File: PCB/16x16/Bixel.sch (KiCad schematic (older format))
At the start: 256 parts

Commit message: Starting the wiring in the schematic
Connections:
- net COL_0: now also B1.10 (COL), B10.10 (COL), B11.10 (COL), B12.10 (COL), B13.10 (COL), B14.10 (COL), B15.10 (COL), B16.10 (COL), B2.10 (COL), B3.10 (COL), B4.10 (COL), B5.10 (COL)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
- net COL_1: now also B17.10 (COL), B18.10 (COL), B19.10 (COL), B20.10 (COL), B21.10 (COL), B22.10 (COL), B23.10 (COL), B24.10 (COL), B25.10 (COL), B26.10 (COL), B27.10 (COL), B28.10 (COL)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
- net COL_10: now also B161.10 (COL), B162.10 (COL), B163.10 (COL), B164.10 (COL), B165.10 (COL), B166.10 (COL), B167.10 (COL), B168.10 (COL), B169.10 (COL), B170.10 (COL), B171.10 (COL), B172.10 (COL)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
- net COL_11: now also B177.10 (COL), B178.10 (COL), B179.10 (COL), B180.10 (COL), B181.10 (COL), B182.10 (COL), B183.10 (COL), B184.10 (COL), B185.10 (COL), B186.10 (COL), B187.10 (COL), B188.10 (COL)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
- net COL_12: now also B193.10 (COL), B194.10 (COL), B195.10 (COL), B196.10 (COL), B197.10 (COL), B198.10 (COL), B199.10 (COL), B200.10 (COL), B201.10 (COL), B202.10 (COL), B203.10 (COL), B204.10 (COL)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
- net COL_13: now also B209.10 (COL), B210.10 (COL), B211.10 (COL), B212.10 (COL), B213.10 (COL), B214.10 (COL), B215.10 (COL), B216.10 (COL), B217.10 (COL), B218.10 (COL), B219.10 (COL), B220.10 (COL)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
- net COL_14: now also B225.10 (COL), B226.10 (COL), B227.10 (COL), B228.10 (COL), B229.10 (COL), B230.10 (COL), B231.10 (COL), B232.10 (COL), B233.10 (COL), B234.10 (COL), B235.10 (COL), B236.10 (COL)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
- net COL_15: now also B241.10 (COL), B242.10 (COL), B243.10 (COL), B244.10 (COL), B245.10 (COL), B246.10 (COL), B247.10 (COL), B248.10 (COL), B249.10 (COL), B250.10 (COL), B251.10 (COL), B252.10 (COL)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
- net COL_2: now also B33.10 (COL), B34.10 (COL), B35.10 (COL), B36.10 (COL), B37.10 (COL), B38.10 (COL), B39.10 (COL), B40.10 (COL), B41.10 (COL), B42.10 (COL), B43.10 (COL), B44.10 (COL)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
- net COL_3: now also B49.10 (COL), B50.10 (COL), B51.10 (COL), B52.10 (COL), B53.10 (COL), B54.10 (COL), B55.10 (COL), B56.10 (COL), B57.10 (COL), B58.10 (COL), B59.10 (COL), B60.10 (COL)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
- net COL_4: now also B65.10 (COL), B66.10 (COL), B67.10 (COL), B68.10 (COL), B69.10 (COL), B70.10 (COL), B71.10 (COL), B72.10 (COL), B73.10 (COL), B74.10 (COL), B75.10 (COL), B76.10 (COL)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
- net COL_5: now also B81.10 (COL), B82.10 (COL), B83.10 (COL), B84.10 (COL), B85.10 (COL), B86.10 (COL), B87.10 (COL), B88.10 (COL), B89.10 (COL), B90.10 (COL), B91.10 (COL), B92.10 (COL)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
- net COL_6: now also B100.10 (COL), B101.10 (COL), B102.10 (COL), B103.10 (COL), B104.10 (COL), B105.10 (COL), B106.10 (COL), B107.10 (COL), B108.10 (COL), B109.10 (COL), B110.10 (COL), B111.10 (COL)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
- net COL_7: now also B113.10 (COL), B114.10 (COL), B115.10 (COL), B116.10 (COL), B117.10 (COL), B118.10 (COL), B119.10 (COL), B120.10 (COL), B121.10 (COL), B122.10 (COL), B123.10 (COL), B124.10 (COL)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
- net COL_8: now also B129.10 (COL), B130.10 (COL), B131.10 (COL), B132.10 (COL), B133.10 (COL), B134.10 (COL), B135.10 (COL), B136.10 (COL), B137.10 (COL), B138.10 (COL), B139.10 (COL), B140.10 (COL)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
- net COL_9: now also B145.10 (COL), B146.10 (COL), B147.10 (COL), B148.10 (COL), B149.10 (COL), B150.10 (COL), B151.10 (COL), B152.10 (COL), B153.10 (COL), B154.10 (COL), B155.10 (COL), B156.10 (COL)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
- net ROW_0: now also B1.9 (ROW), B113.9 (ROW), B129.9 (ROW), B145.9 (ROW), B161.9 (ROW), B17.9 (ROW), B177.9 (ROW), B193.9 (ROW), B209.9 (ROW), B225.9 (ROW), B241.9 (ROW), B33.9 (ROW)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
- net ROW_1: now also B114.9 (ROW), B130.9 (ROW), B146.9 (ROW), B162.9 (ROW), B178.9 (ROW), B18.9 (ROW), B194.9 (ROW), B2.9 (ROW), B210.9 (ROW), B226.9 (ROW), B242.9 (ROW), B34.9 (ROW)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
- net ROW_10: now also B107.9 (ROW), B11.9 (ROW), B123.9 (ROW), B139.9 (ROW), B155.9 (ROW), B171.9 (ROW), B187.9 (ROW), B203.9 (ROW), B219.9 (ROW), B235.9 (ROW), B251.9 (ROW), B27.9 (ROW)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
- net ROW_11: now also B108.9 (ROW), B12.9 (ROW), B124.9 (ROW), B140.9 (ROW), B156.9 (ROW), B172.9 (ROW), B188.9 (ROW), B204.9 (ROW), B220.9 (ROW), B236.9 (ROW), B252.9 (ROW), B28.9 (ROW)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
- net ROW_12: now also B109.9 (ROW), B125.9 (ROW), B13.9 (ROW), B157.9 (ROW), B173.9 (ROW), B189.9 (ROW), B205.9 (ROW), B221.9 (ROW), B237.9 (ROW), B253.9 (ROW), B29.9 (ROW), B45.9 (ROW)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
- net ROW_13: now also B110.9 (ROW), B126.9 (ROW), B14.9 (ROW), B142.9 (ROW), B158.9 (ROW), B174.9 (ROW), B190.9 (ROW), B206.9 (ROW), B222.9 (ROW), B238.9 (ROW), B254.9 (ROW), B30.9 (ROW)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
- net ROW_14: now also B111.9 (ROW), B127.9 (ROW), B143.9 (ROW), B15.9 (ROW), B159.9 (ROW), B175.9 (ROW), B191.9 (ROW), B207.9 (ROW), B223.9 (ROW), B239.9 (ROW), B255.9 (ROW), B31.9 (ROW)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
- net ROW_15: now also B112.9 (ROW), B128.9 (ROW), B144.9 (ROW), B16.9 (ROW), B160.9 (ROW), B176.9 (ROW), B192.9 (ROW), B208.9 (ROW), B224.9 (ROW), B240.9 (ROW), B256.9 (ROW), B32.9 (ROW)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
- net ROW_2: now also B115.9 (ROW), B131.9 (ROW), B147.9 (ROW), B163.9 (ROW), B179.9 (ROW), B19.9 (ROW), B195.9 (ROW), B211.9 (ROW), B227.9 (ROW), B243.9 (ROW), B3.9 (ROW), B35.9 (ROW)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
- net ROW_3: now also B100.9 (ROW), B116.9 (ROW), B132.9 (ROW), B148.9 (ROW), B164.9 (ROW), B180.9 (ROW), B196.9 (ROW), B20.9 (ROW), B212.9 (ROW), B228.9 (ROW), B244.9 (ROW), B36.9 (ROW)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
- net ROW_4: now also B101.9 (ROW), B117.9 (ROW), B133.9 (ROW), B149.9 (ROW), B165.9 (ROW), B181.9 (ROW), B197.9 (ROW), B21.9 (ROW), B213.9 (ROW), B229.9 (ROW), B245.9 (ROW), B37.9 (ROW)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
- net ROW_5: now also B102.9 (ROW), B118.9 (ROW), B134.9 (ROW), B150.9 (ROW), B166.9 (ROW), B182.9 (ROW), B198.9 (ROW), B214.9 (ROW), B22.9 (ROW), B230.9 (ROW), B246.9 (ROW), B38.9 (ROW)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
- net ROW_6: now also B103.9 (ROW), B119.9 (ROW), B135.9 (ROW), B151.9 (ROW), B167.9 (ROW), B183.9 (ROW), B199.9 (ROW), B215.9 (ROW), B23.9 (ROW), B231.9 (ROW), B247.9 (ROW), B39.9 (ROW)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
- net ROW_7: now also B104.9 (ROW), B120.9 (ROW), B136.9 (ROW), B152.9 (ROW), B168.9 (ROW), B184.9 (ROW), B200.9 (ROW), B216.9 (ROW), B232.9 (ROW), B24.9 (ROW), B248.9 (ROW), B40.9 (ROW)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
- net ROW_8: now also B105.9 (ROW), B121.9 (ROW), B137.9 (ROW), B153.9 (ROW), B169.9 (ROW), B185.9 (ROW), B201.9 (ROW), B217.9 (ROW), B233.9 (ROW), B249.9 (ROW), B25.9 (ROW), B41.9 (ROW)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
- net ROW_9: now also B10.9 (ROW), B106.9 (ROW), B122.9 (ROW), B138.9 (ROW), B154.9 (ROW), B170.9 (ROW), B186.9 (ROW), B202.9 (ROW), B218.9 (ROW), B234.9 (ROW), B250.9 (ROW), B26.9 (ROW)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
- net at B1.5 (VCC): now also B2.1 (VCC)
- net at B1.6 (CO): now also B2.2 (CI)
- net at B1.7 (DO): now also B2.3 (DI)
- net at B1.8 (GND): now also B2.4 (GND)
- net at B2.5 (VCC): now also B3.1 (VCC)
- net at B2.6 (CO): now also B3.2 (CI)
- net at B2.7 (DO): now also B3.3 (DI)
- net at B2.8 (GND): now also B3.4 (GND)
- net at B3.5 (VCC): now also B4.1 (VCC)
- net at B3.6 (CO): now also B4.2 (CI)
- net at B3.7 (DO): now also B4.3 (DI)
- net at B3.8 (GND): now also B4.4 (GND)
- net at B4.5 (VCC): now also B5.1 (VCC)
- net at B4.6 (CO): now also B5.2 (CI)
- net at B4.7 (DO): now also B5.3 (DI)
- net at B4.8 (GND): now also B5.4 (GND)
- net at B5.5 (VCC): now also B6.1 (VCC)
- net at B5.6 (CO): now also B6.2 (CI)
- net at B5.7 (DO): now also B6.3 (DI)
- net at B5.8 (GND): now also B6.4 (GND)
- net at B6.5 (VCC): now also B7.1 (VCC)
- net at B6.6 (CO): now also B7.2 (CI)
- net at B6.7 (DO): now also B7.3 (DI)
- net at B6.8 (GND): now also B7.4 (GND)
- net at B7.5 (VCC): now also B8.1 (VCC)
- net at B7.6 (CO): now also B8.2 (CI)
- net at B7.7 (DO): now also B8.3 (DI)
- net at B7.8 (GND): now also B8.4 (GND)
- net at B8.5 (VCC): now also B9.1 (VCC)
- net at B8.6 (CO): now also B9.2 (CI)
- net at B8.7 (DO): now also B9.3 (DI)
- net at B8.8 (GND): now also B9.4 (GND)
- net at B9.5 (VCC): now also B10.1 (VCC)
- net at B9.6 (CO): now also B10.2 (CI)
- net at B9.7 (DO): now also B10.3 (DI)
- net at B9.8 (GND): now also B10.4 (GND)
- net at B10.5 (VCC): now also B11.1 (VCC)
- net at B10.6 (CO): now also B11.2 (CI)
- net at B10.7 (DO): now also B11.3 (DI)
- net at B10.8 (GND): now also B11.4 (GND)
- net at B11.5 (VCC): now also B12.1 (VCC)
- net at B11.6 (CO): now also B12.2 (CI)
- net at B11.7 (DO): now also B12.3 (DI)
- net at B11.8 (GND): now also B12.4 (GND)
- net at B12.5 (VCC): now also B13.1 (VCC)
- net at B12.6 (CO): now also B13.2 (CI)
- net at B12.7 (DO): now also B13.3 (DI)
- net at B12.8 (GND): now also B13.4 (GND)
- net at B13.5 (VCC): now also B14.1 (VCC)
- net at B13.6 (CO): now also B14.2 (CI)
- net at B13.7 (DO): now also B14.3 (DI)
- net at B13.8 (GND): now also B14.4 (GND)
- net at B14.5 (VCC): now also B15.1 (VCC)
- net at B14.6 (CO): now also B15.2 (CI)
- net at B14.7 (DO): now also B15.3 (DI)
- net at B14.8 (GND): now also B15.4 (GND)
- net at B15.5 (VCC): now also B16.1 (VCC)
- net at B15.6 (CO): now also B16.2 (CI)
- net at B15.7 (DO): now also B16.3 (DI)
- net at B15.8 (GND): now also B16.4 (GND)
- net at B16.5 (VCC): now also B32.8 (VCC)
- net at B16.6 (CO): now also B32.7 (CI)
- net at B16.7 (DO): now also B32.6 (DI)
- net at B16.8 (GND): now also B32.5 (GND)
- net at B17.1 (GND): now also B33.4 (GND)
- net at B17.2 (DO): now also B33.3 (DI)
- net at B17.3 (CO): now also B33.2 (CI)
- net at B17.4 (VCC): now also B33.1 (VCC)
- net at B17.5 (GND): now also B18.1 (GND)
- net at B17.6 (DI): now also B18.2 (DO)
- net at B17.7 (CI): now also B18.3 (CO)
- net at B17.8 (VCC): now also B18.4 (VCC)
- net at B18.5 (GND): now also B19.1 (GND)
- net at B18.6 (DI): now also B19.2 (DO)
- net at B18.7 (CI): now also B19.3 (CO)
- net at B18.8 (VCC): now also B19.4 (VCC)
- net at B19.5 (GND): now also B20.1 (GND)
- net at B19.6 (DI): now also B20.2 (DO)
- net at B19.7 (CI): now also B20.3 (CO)
- net at B19.8 (VCC): now also B20.4 (VCC)
- net at B20.5 (GND): now also B21.1 (GND)
- net at B20.6 (DI): now also B21.2 (DO)
- net at B20.7 (CI): now also B21.3 (CO)
- net at B20.8 (VCC): now also B21.4 (VCC)
- net at B21.5 (GND): now also B22.1 (GND)
- net at B21.6 (DI): now also B22.2 (DO)
- net at B21.7 (CI): now also B22.3 (CO)
- net at B21.8 (VCC): now also B22.4 (VCC)
- net at B22.5 (GND): now also B23.1 (GND)
- net at B22.6 (DI): now also B23.2 (DO)
- net at B22.7 (CI): now also B23.3 (CO)
- net at B22.8 (VCC): now also B23.4 (VCC)
- net at B23.5 (GND): now also B24.1 (GND)
- net at B23.6 (DI): now also B24.2 (DO)
- net at B23.7 (CI): now also B24.3 (CO)
- net at B23.8 (VCC): now also B24.4 (VCC)
- net at B24.5 (GND): now also B25.1 (GND)
- net at B24.6 (DI): now also B25.2 (DO)
- net at B24.7 (CI): now also B25.3 (CO)
- net at B24.8 (VCC): now also B25.4 (VCC)
- net at B25.5 (GND): now also B26.1 (GND)
- net at B25.6 (DI): now also B26.2 (DO)
- net at B25.7 (CI): now also B26.3 (CO)
- net at B25.8 (VCC): now also B26.4 (VCC)
- net at B26.5 (GND): now also B27.1 (GND)
- net at B26.6 (DI): now also B27.2 (DO)
- net at B26.7 (CI): now also B27.3 (CO)
- net at B26.8 (VCC): now also B27.4 (VCC)
- net at B27.5 (GND): now also B28.1 (GND)
- net at B27.6 (DI): now also B28.2 (DO)
- net at B27.7 (CI): now also B28.3 (CO)
- net at B27.8 (VCC): now also B28.4 (VCC)
- net at B28.5 (GND): now also B29.1 (GND)
- net at B28.6 (DI): now also B29.2 (DO)
- net at B28.7 (CI): now also B29.3 (CO)
- net at B28.8 (VCC): now also B29.4 (VCC)
- net at B29.5 (GND): now also B30.1 (GND)
- net at B29.6 (DI): now also B30.2 (DO)
- net at B29.7 (CI): now also B30.3 (CO)
- net at B29.8 (VCC): now also B30.4 (VCC)
- net at B30.5 (GND): now also B31.1 (GND)
- net at B30.6 (DI): now also B31.2 (DO)
- net at B30.7 (CI): now also B31.3 (CO)
- net at B30.8 (VCC): now also B31.4 (VCC)
- net at B31.5 (GND): now also B32.1 (GND)
- net at B31.6 (DI): now also B32.2 (DO)
- net at B31.7 (CI): now also B32.3 (CO)
- net at B31.8 (VCC): now also B32.4 (VCC)
- net at B33.5 (VCC): now also B34.1 (VCC)
- net at B33.6 (CO): now also B34.2 (CI)
- net at B33.7 (DO): now also B34.3 (DI)
- net at B33.8 (GND): now also B34.4 (GND)
- net at B34.5 (VCC): now also B35.1 (VCC)
- net at B34.6 (CO): now also B35.2 (CI)
- net at B34.7 (DO): now also B35.3 (DI)
- net at B34.8 (GND): now also B35.4 (GND)
- net at B35.5 (VCC): now also B36.1 (VCC)
- net at B35.6 (CO): now also B36.2 (CI)
- net at B35.7 (DO): now also B36.3 (DI)
- net at B35.8 (GND): now also B36.4 (GND)
- net at B36.5 (VCC): now also B37.1 (VCC)
- net at B36.6 (CO): now also B37.2 (CI)
- net at B36.7 (DO): now also B37.3 (DI)
- net at B36.8 (GND): now also B37.4 (GND)
- net at B37.5 (VCC): now also B38.1 (VCC)
- net at B37.6 (CO): now also B38.2 (CI)
- net at B37.7 (DO): now also B38.3 (DI)
- net at B37.8 (GND): now also B38.4 (GND)
- net at B38.5 (VCC): now also B39.1 (VCC)
- net at B38.6 (CO): now also B39.2 (CI)
- net at B38.7 (DO): now also B39.3 (DI)
- net at B38.8 (GND): now also B39.4 (GND)
- net at B39.5 (VCC): now also B40.1 (VCC)
- net at B39.6 (CO): now also B40.2 (CI)
- net at B39.7 (DO): now also B40.3 (DI)
- net at B39.8 (GND): now also B40.4 (GND)
- net at B40.5 (VCC): now also B41.1 (VCC)
- net at B40.6 (CO): now also B41.2 (CI)
- net at B40.7 (DO): now also B41.3 (DI)
- net at B40.8 (GND): now also B41.4 (GND)
- net at B41.5 (VCC): now also B42.1 (VCC)
- net at B41.6 (CO): now also B42.2 (CI)
- net at B41.7 (DO): now also B42.3 (DI)
- net at B41.8 (GND): now also B42.4 (GND)
- net at B42.5 (VCC): now also B43.1 (VCC)
- net at B42.6 (CO): now also B43.2 (CI)
- net at B42.7 (DO): now also B43.3 (DI)
- net at B42.8 (GND): now also B43.4 (GND)
- net at B43.5 (VCC): now also B44.1 (VCC)
- net at B43.6 (CO): now also B44.2 (CI)
- net at B43.7 (DO): now also B44.3 (DI)
- net at B43.8 (GND): now also B44.4 (GND)
- net at B44.5 (VCC): now also B45.1 (VCC)
- net at B44.6 (CO): now also B45.2 (CI)
- net at B44.7 (DO): now also B45.3 (DI)
- net at B44.8 (GND): now also B45.4 (GND)
- net at B45.5 (VCC): now also B46.1 (VCC)
- net at B45.6 (CO): now also B46.2 (CI)
- net at B45.7 (DO): now also B46.3 (DI)
- net at B45.8 (GND): now also B46.4 (GND)
- net at B46.5 (VCC): now also B47.1 (VCC)
- net at B46.6 (CO): now also B47.2 (CI)
- net at B46.7 (DO): now also B47.3 (DI)
- net at B46.8 (GND): now also B47.4 (GND)
- net at B47.5 (VCC): now also B48.1 (VCC)
- net at B47.6 (CO): now also B48.2 (CI)
- net at B47.7 (DO): now also B48.3 (DI)
- net at B47.8 (GND): now also B48.4 (GND)
- net at B48.5 (VCC): now also B64.8 (VCC)
- net at B48.6 (CO): now also B64.7 (CI)
- net at B48.7 (DO): now also B64.6 (DI)
- net at B48.8 (GND): now also B64.5 (GND)
- net at B49.1 (GND): now also B65.4 (GND)
- net at B49.2 (DO): now also B65.3 (DI)
- net at B49.3 (CO): now also B65.2 (CI)
- net at B49.4 (VCC): now also B65.1 (VCC)
- net at B49.5 (GND): now also B50.1 (GND)
- net at B49.6 (DI): now also B50.2 (DO)
- net at B49.7 (CI): now also B50.3 (CO)
- net at B49.8 (VCC): now also B50.4 (VCC)
- net at B50.5 (GND): now also B51.1 (GND)
- net at B50.6 (DI): now also B51.2 (DO)
- net at B50.7 (CI): now also B51.3 (CO)
- net at B50.8 (VCC): now also B51.4 (VCC)
- net at B51.5 (GND): now also B52.1 (GND)
- net at B51.6 (DI): now also B52.2 (DO)
- net at B51.7 (CI): now also B52.3 (CO)
- net at B51.8 (VCC): now also B52.4 (VCC)
- net at B52.5 (GND): now also B53.1 (GND)
- net at B52.6 (DI): now also B53.2 (DO)
- net at B52.7 (CI): now also B53.3 (CO)
- net at B52.8 (VCC): now also B53.4 (VCC)
- net at B53.5 (GND): now also B54.1 (GND)
- net at B53.6 (DI): now also B54.2 (DO)
- net at B53.7 (CI): now also B54.3 (CO)
- net at B53.8 (VCC): now also B54.4 (VCC)
- net at B54.5 (GND): now also B55.1 (GND)
- net at B54.6 (DI): now also B55.2 (DO)
- net at B54.7 (CI): now also B55.3 (CO)
- net at B54.8 (VCC): now also B55.4 (VCC)
- net at B55.5 (GND): now also B56.1 (GND)
- net at B55.6 (DI): now also B56.2 (DO)
- net at B55.7 (CI): now also B56.3 (CO)
- net at B55.8 (VCC): now also B56.4 (VCC)
- net at B56.5 (GND): now also B57.1 (GND)
- net at B56.6 (DI): now also B57.2 (DO)
- net at B56.7 (CI): now also B57.3 (CO)
- net at B56.8 (VCC): now also B57.4 (VCC)
- net at B57.5 (GND): now also B58.1 (GND)
- net at B57.6 (DI): now also B58.2 (DO)
- net at B57.7 (CI): now also B58.3 (CO)
- net at B57.8 (VCC): now also B58.4 (VCC)
- net at B58.5 (GND): now also B59.1 (GND)
- net at B58.6 (DI): now also B59.2 (DO)
- net at B58.7 (CI): now also B59.3 (CO)
- net at B58.8 (VCC): now also B59.4 (VCC)
- net at B59.5 (GND): now also B60.1 (GND)
- net at B59.6 (DI): now also B60.2 (DO)
- net at B59.7 (CI): now also B60.3 (CO)
- net at B59.8 (VCC): now also B60.4 (VCC)
- net at B60.5 (GND): now also B61.1 (GND)
- net at B60.6 (DI): now also B61.2 (DO)
- net at B60.7 (CI): now also B61.3 (CO)
- net at B60.8 (VCC): now also B61.4 (VCC)
- net at B61.5 (GND): now also B62.1 (GND)
- net at B61.6 (DI): now also B62.2 (DO)
- net at B61.7 (CI): now also B62.3 (CO)
- net at B61.8 (VCC): now also B62.4 (VCC)
- net at B62.5 (GND): now also B63.1 (GND)
- net at B62.6 (DI): now also B63.2 (DO)
- net at B62.7 (CI): now also B63.3 (CO)
- net at B62.8 (VCC): now also B63.4 (VCC)
- net at B63.5 (GND): now also B64.1 (GND)
- net at B63.6 (DI): now also B64.2 (DO)
- net at B63.7 (CI): now also B64.3 (CO)
- net at B63.8 (VCC): now also B64.4 (VCC)
- net at B65.5 (VCC): now also B66.1 (VCC)
- net at B65.6 (CO): now also B66.2 (CI)
- net at B65.7 (DO): now also B66.3 (DI)
- net at B65.8 (GND): now also B66.4 (GND)
- net at B66.5 (VCC): now also B67.1 (VCC)
- net at B66.6 (CO): now also B67.2 (CI)
- net at B66.7 (DO): now also B67.3 (DI)
- net at B66.8 (GND): now also B67.4 (GND)
- net at B67.5 (VCC): now also B68.1 (VCC)
- net at B67.6 (CO): now also B68.2 (CI)
- net at B67.7 (DO): now also B68.3 (DI)
- net at B67.8 (GND): now also B68.4 (GND)
- net at B68.5 (VCC): now also B69.1 (VCC)
- net at B68.6 (CO): now also B69.2 (CI)
- net at B68.7 (DO): now also B69.3 (DI)
- net at B68.8 (GND): now also B69.4 (GND)
- net at B69.5 (VCC): now also B70.1 (VCC)
- net at B69.6 (CO): now also B70.2 (CI)
- net at B69.7 (DO): now also B70.3 (DI)
- net at B69.8 (GND): now also B70.4 (GND)
- net at B70.5 (VCC): now also B71.1 (VCC)
- net at B70.6 (CO): now also B71.2 (CI)
- net at B70.7 (DO): now also B71.3 (DI)
- net at B70.8 (GND): now also B71.4 (GND)
- net at B71.5 (VCC): now also B72.1 (VCC)
- net at B71.6 (CO): now also B72.2 (CI)
- net at B71.7 (DO): now also B72.3 (DI)
- net at B71.8 (GND): now also B72.4 (GND)
- net at B72.5 (VCC): now also B73.1 (VCC)
- net at B72.6 (CO): now also B73.2 (CI)
- net at B72.7 (DO): now also B73.3 (DI)
- net at B72.8 (GND): now also B73.4 (GND)
- net at B73.5 (VCC): now also B74.1 (VCC)
- net at B73.6 (CO): now also B74.2 (CI)
- net at B73.7 (DO): now also B74.3 (DI)
- net at B73.8 (GND): now also B74.4 (GND)
- net at B74.5 (VCC): now also B75.1 (VCC)
- net at B74.6 (CO): now also B75.2 (CI)
- net at B74.7 (DO): now also B75.3 (DI)
- net at B74.8 (GND): now also B75.4 (GND)
- net at B75.5 (VCC): now also B76.1 (VCC)
- net at B75.6 (CO): now also B76.2 (CI)
- net at B75.7 (DO): now also B76.3 (DI)
- net at B75.8 (GND): now also B76.4 (GND)
- net at B76.5 (VCC): now also B77.1 (VCC)
- net at B76.6 (CO): now also B77.2 (CI)
- net at B76.7 (DO): now also B77.3 (DI)
- net at B76.8 (GND): now also B77.4 (GND)
- net at B77.5 (VCC): now also B78.1 (VCC)
- net at B77.6 (CO): now also B78.2 (CI)
- net at B77.7 (DO): now also B78.3 (DI)
- net at B77.8 (GND): now also B78.4 (GND)
- net at B78.5 (VCC): now also B79.1 (VCC)
- net at B78.6 (CO): now also B79.2 (CI)
- net at B78.7 (DO): now also B79.3 (DI)
- net at B78.8 (GND): now also B79.4 (GND)
- net at B79.5 (VCC): now also B80.1 (VCC)
- net at B79.6 (CO): now also B80.2 (CI)
- net at B79.7 (DO): now also B80.3 (DI)
- net at B79.8 (GND): now also B80.4 (GND)
- net at B80.5 (VCC): now also B96.8 (VCC)
- net at B80.6 (CO): now also B96.7 (CI)
- net at B80.7 (DO): now also B96.6 (DI)
- net at B80.8 (GND): now also B96.5 (GND)
- net at B81.1 (GND): now also B97.4 (GND)
- net at B81.2 (DO): now also B97.3 (DI)
- net at B81.3 (CO): now also B97.2 (CI)
- net at B81.4 (VCC): now also B97.1 (VCC)
- net at B81.5 (GND): now also B82.1 (GND)
- net at B81.6 (DI): now also B82.2 (DO)
- net at B81.7 (CI): now also B82.3 (CO)
- net at B81.8 (VCC): now also B82.4 (VCC)
- net at B82.5 (GND): now also B83.1 (GND)
- net at B82.6 (DI): now also B83.2 (DO)
- net at B82.7 (CI): now also B83.3 (CO)
- net at B82.8 (VCC): now also B83.4 (VCC)
- net at B83.5 (GND): now also B84.1 (GND)
- net at B83.6 (DI): now also B84.2 (DO)
- net at B83.7 (CI): now also B84.3 (CO)
- net at B83.8 (VCC): now also B84.4 (VCC)
- net at B84.5 (GND): now also B85.1 (GND)
- net at B84.6 (DI): now also B85.2 (DO)
- net at B84.7 (CI): now also B85.3 (CO)
- net at B84.8 (VCC): now also B85.4 (VCC)
- net at B85.5 (GND): now also B86.1 (GND)
- net at B85.6 (DI): now also B86.2 (DO)
- net at B85.7 (CI): now also B86.3 (CO)
- net at B85.8 (VCC): now also B86.4 (VCC)
- net at B86.5 (GND): now also B87.1 (GND)
- net at B86.6 (DI): now also B87.2 (DO)
- net at B86.7 (CI): now also B87.3 (CO)
- net at B86.8 (VCC): now also B87.4 (VCC)
- net at B87.5 (GND): now also B88.1 (GND)
- net at B87.6 (DI): now also B88.2 (DO)
- net at B87.7 (CI): now also B88.3 (CO)
- net at B87.8 (VCC): now also B88.4 (VCC)
- net at B88.5 (GND): now also B89.1 (GND)
- net at B88.6 (DI): now also B89.2 (DO)
- net at B88.7 (CI): now also B89.3 (CO)
- net at B88.8 (VCC): now also B89.4 (VCC)
- net at B89.5 (GND): now also B90.1 (GND)
- net at B89.6 (DI): now also B90.2 (DO)
- net at B89.7 (CI): now also B90.3 (CO)
- net at B89.8 (VCC): now also B90.4 (VCC)
- net at B90.5 (GND): now also B91.1 (GND)
- net at B90.6 (DI): now also B91.2 (DO)
- net at B90.7 (CI): now also B91.3 (CO)
- net at B90.8 (VCC): now also B91.4 (VCC)
- net at B91.5 (GND): now also B92.1 (GND)
- net at B91.6 (DI): now also B92.2 (DO)
- net at B91.7 (CI): now also B92.3 (CO)
- net at B91.8 (VCC): now also B92.4 (VCC)
- net at B92.5 (GND): now also B93.1 (GND)
- net at B92.6 (DI): now also B93.2 (DO)
- net at B92.7 (CI): now also B93.3 (CO)
- net at B92.8 (VCC): now also B93.4 (VCC)
- net at B93.5 (GND): now also B94.1 (GND)
- net at B93.6 (DI): now also B94.2 (DO)
- net at B93.7 (CI): now also B94.3 (CO)
- net at B93.8 (VCC): now also B94.4 (VCC)
- net at B94.5 (GND): now also B95.1 (GND)
- net at B94.6 (DI): now also B95.2 (DO)
- net at B94.7 (CI): now also B95.3 (CO)
- net at B94.8 (VCC): now also B95.4 (VCC)
- net at B95.5 (GND): now also B96.1 (GND)
- net at B95.6 (DI): now also B96.2 (DO)
- net at B95.7 (CI): now also B96.3 (CO)
- net at B95.8 (VCC): now also B96.4 (VCC)
- net at B97.5 (VCC): now also B98.1 (VCC)
- net at B97.6 (CO): now also B98.2 (CI)
- net at B97.7 (DO): now also B98.3 (DI)
- net at B97.8 (GND): now also B98.4 (GND)
- net at B98.5 (VCC): now also B99.1 (VCC)
- net at B98.6 (CO): now also B99.2 (CI)
- net at B98.7 (DO): now also B99.3 (DI)
- net at B98.8 (GND): now also B99.4 (GND)
- net at B99.5 (VCC): now also B100.1 (VCC)
- net at B99.6 (CO): now also B100.2 (CI)
- net at B99.7 (DO): now also B100.3 (DI)
- net at B99.8 (GND): now also B100.4 (GND)
- net at B100.5 (VCC): now also B101.1 (VCC)
- net at B100.6 (CO): now also B101.2 (CI)
- net at B100.7 (DO): now also B101.3 (DI)
- net at B100.8 (GND): now also B101.4 (GND)
- net at B101.5 (VCC): now also B102.1 (VCC)
- net at B101.6 (CO): now also B102.2 (CI)
- net at B101.7 (DO): now also B102.3 (DI)
- net at B101.8 (GND): now also B102.4 (GND)
- net at B102.5 (VCC): now also B103.1 (VCC)
- net at B102.6 (CO): now also B103.2 (CI)
- net at B102.7 (DO): now also B103.3 (DI)
- net at B102.8 (GND): now also B103.4 (GND)
- net at B103.5 (VCC): now also B104.1 (VCC)
- net at B103.6 (CO): now also B104.2 (CI)
- net at B103.7 (DO): now also B104.3 (DI)
- net at B103.8 (GND): now also B104.4 (GND)
- net at B104.5 (VCC): now also B105.1 (VCC)
- net at B104.6 (CO): now also B105.2 (CI)
- net at B104.7 (DO): now also B105.3 (DI)
- net at B104.8 (GND): now also B105.4 (GND)
- net at B105.5 (VCC): now also B106.1 (VCC)
- net at B105.6 (CO): now also B106.2 (CI)
- net at B105.7 (DO): now also B106.3 (DI)
- net at B105.8 (GND): now also B106.4 (GND)
- net at B106.5 (VCC): now also B107.1 (VCC)
- net at B106.6 (CO): now also B107.2 (CI)
- net at B106.7 (DO): now also B107.3 (DI)
- net at B106.8 (GND): now also B107.4 (GND)
- net at B107.5 (VCC): now also B108.1 (VCC)
- net at B107.6 (CO): now also B108.2 (CI)
- net at B107.7 (DO): now also B108.3 (DI)
- net at B107.8 (GND): now also B108.4 (GND)
- net at B108.5 (VCC): now also B109.1 (VCC)
- net at B108.6 (CO): now also B109.2 (CI)
- net at B108.7 (DO): now also B109.3 (DI)
- net at B108.8 (GND): now also B109.4 (GND)
- net at B109.5 (VCC): now also B110.1 (VCC)
- net at B109.6 (CO): now also B110.2 (CI)
- net at B109.7 (DO): now also B110.3 (DI)
- net at B109.8 (GND): now also B110.4 (GND)
- net at B110.5 (VCC): now also B111.1 (VCC)
- net at B110.6 (CO): now also B111.2 (CI)
- net at B110.7 (DO): now also B111.3 (DI)
- net at B110.8 (GND): now also B111.4 (GND)
- net at B111.5 (VCC): now also B112.1 (VCC)
- net at B111.6 (CO): now also B112.2 (CI)
- net at B111.7 (DO): now also B112.3 (DI)
- net at B111.8 (GND): now also B112.4 (GND)
- net at B112.5 (VCC): now also B128.8 (VCC)
- net at B112.6 (CO): now also B128.7 (CI)
- net at B112.7 (DO): now also B128.6 (DI)
- net at B112.8 (GND): now also B128.5 (GND)
- net at B113.1 (GND): now also B129.4 (GND)
- net at B113.2 (DO): now also B129.3 (DI)
- net at B113.3 (CO): now also B129.2 (CI)
- net at B113.4 (VCC): now also B129.1 (VCC)
- net at B113.5 (GND): now also B114.1 (GND)
- net at B113.6 (DI): now also B114.2 (DO)
- net at B113.7 (CI): now also B114.3 (CO)
- net at B113.8 (VCC): now also B114.4 (VCC)
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
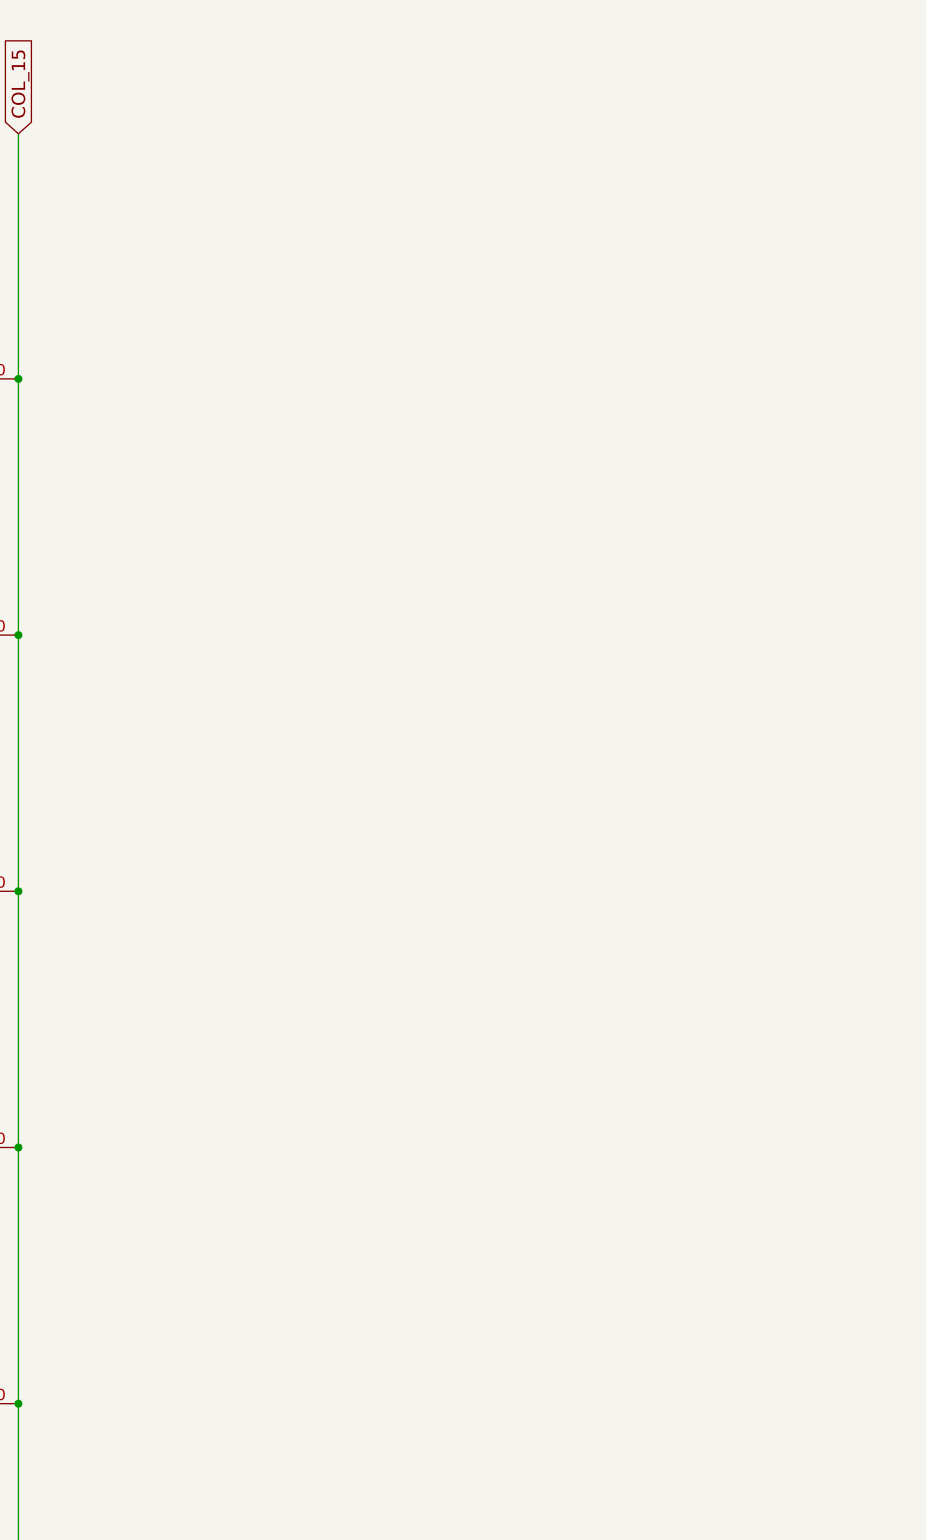
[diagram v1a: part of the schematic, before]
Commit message: Shift Register schematic layout
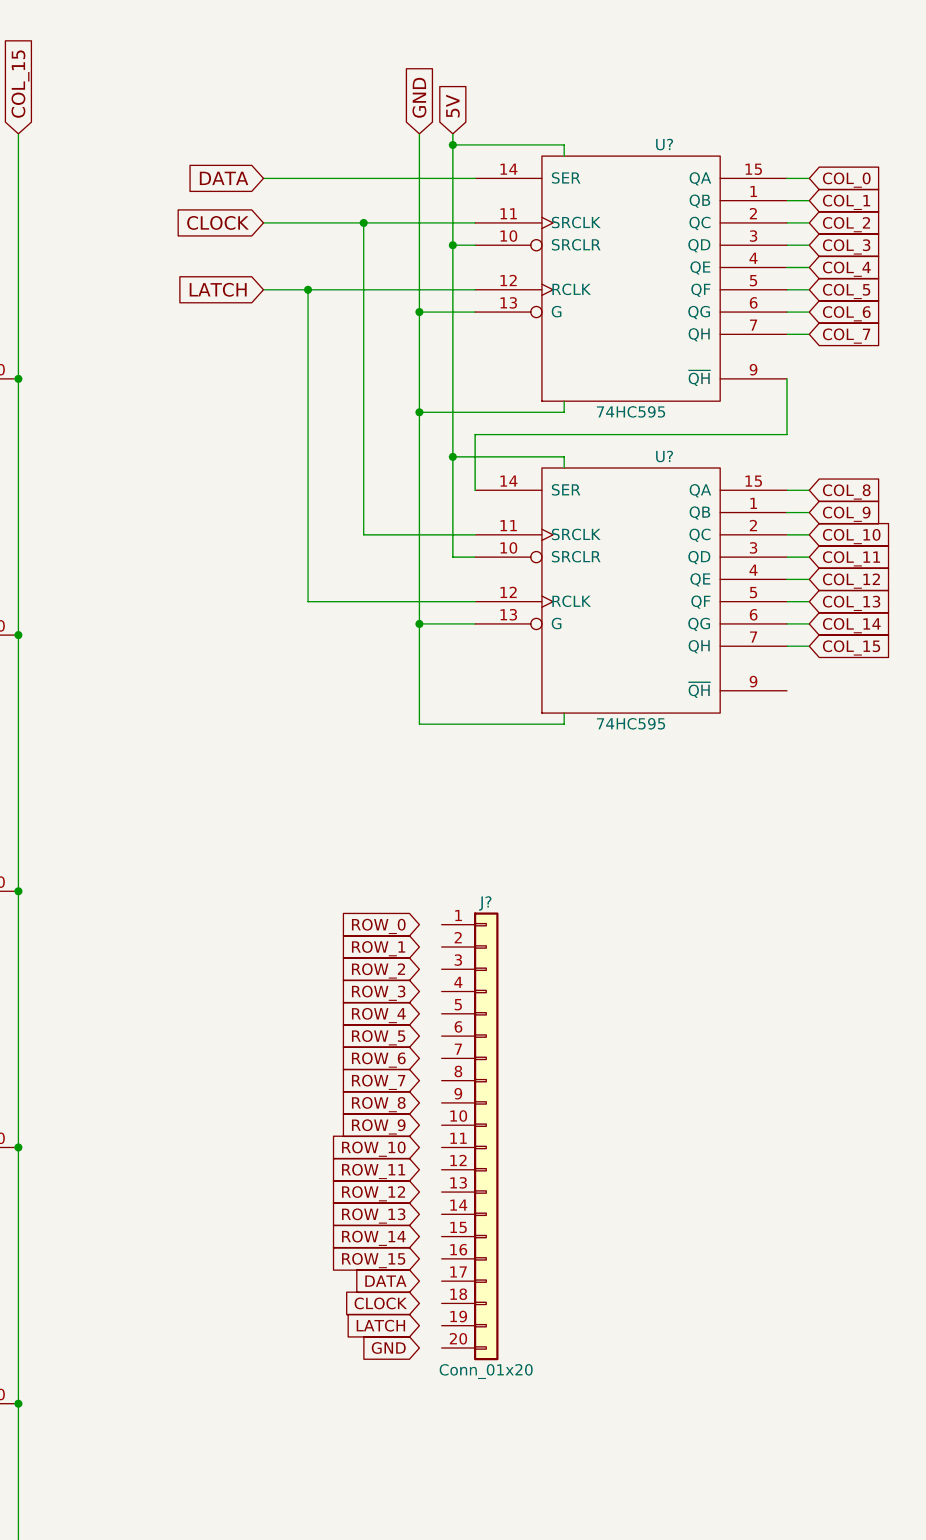
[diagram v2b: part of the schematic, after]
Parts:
- added J?: Conn_01x20, symbol Conn_01x20
- added U? (x2): 74HC595, Housings_DIP:DIP-16_W7.62mm_Socket_LongPads, symbol 74HC595
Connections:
- net COL_0: now also U?.15 (QA)
- net COL_1: now also U?.1 (QB)
- net COL_10: now also U?.2 (QC)
- net COL_11: now also U?.3 (QD)
- net COL_12: now also U?.4 (QE)
- net COL_13: now also U?.5 (QF)
- net COL_14: now also U?.6 (QG)
- net COL_15: now also U?.7 (QH)
- net COL_2: now also U?.2 (QC)
- net COL_3: now also U?.3 (QD)
- net COL_4: now also U?.4 (QE)
- net COL_5: now also U?.5 (QF)
- net COL_6: now also U?.6 (QG)
- net COL_7: now also U?.7 (QH)
- net COL_8: now also U?.15 (QA)
- net COL_9: now also U?.1 (QB)
- new net: U?.14 (SER), U?.9 (~QH)
- new net CLOCK: U?.11 (SRCLK), U?.11 (SRCLK)
- new net DATA: U?.14 (SER)
- new net GND: U?.13 (G), U?.13 (G), U?.8 (GND), U?.8 (GND)
- new net LATCH: U?.12 (RCLK), U?.12 (RCLK)
- new net VCC: U?.10 (SRCLR), U?.10 (SRCLR), U?.16 (VCC), U?.16 (VCC)

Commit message: More work on schematic. Unable to auto-place footprints on PCB.
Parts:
- removed J?: Conn_01x20, symbol Conn_01x20
- added C1: C_Small, Capacitors_THT:C_Disc_D5.0mm_W2.5mm_P2.50mm, symbol C_Small
- added J1: Conn_01x22, Pin_Headers:Pin_Header_Straight_1x22_Pitch2.54mm, symbol Conn_01x22
- added J2: Screw_Terminal_01x02, TerminalBlocks_Phoenix:TerminalBlock_Phoenix_MPT-2.54mm_2pol, symbol Screw_Terminal_01x02
- gave numbers to parts that had none: 2
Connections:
- net VCC is gone; now on net +5V: U1.10 (SRCLR), U1.16 (VCC), U2.10 (SRCLR), U2.16 (VCC)
- net CLOCK: now also J1.18 (Pin_18)
- net DATA: now also J1.17 (Pin_17)
- net GND: now also B1.4 (GND), C1.2, J1.22 (Pin_22), J2.2 (Pin_2)
- net LATCH: now also J1.19 (Pin_19)
- net ROW_0: now also J1.1 (Pin_1)
- net ROW_1: now also J1.2 (Pin_2)
- net ROW_10: now also J1.11 (Pin_11)
- net ROW_11: now also J1.12 (Pin_12)
- net ROW_12: now also B141.9 (ROW), J1.13 (Pin_13)
- net ROW_13: now also J1.14 (Pin_14)
- net ROW_14: now also J1.15 (Pin_15)
- net ROW_15: now also J1.16 (Pin_16)
- net ROW_2: now also J1.3 (Pin_3)
- net ROW_3: now also J1.4 (Pin_4)
- net ROW_4: now also J1.5 (Pin_5)
- net ROW_5: now also J1.6 (Pin_6)
- net ROW_6: now also J1.7 (Pin_7)
- net ROW_7: now also J1.8 (Pin_8)
- net ROW_8: now also J1.9 (Pin_9)
- net ROW_9: now also J1.10 (Pin_10)
- net +5V: now reaches B1.1 (VCC)
- net +5V: now also C1.1, J2.1 (Pin_1)
- net CI: now reaches B1.2 (CI)
- net CI: now also J1.21 (Pin_21)
- net DI: now reaches B1.3 (DI)
- net DI: now also J1.20 (Pin_20)
- no-connect marks 0 -> 5
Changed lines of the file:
@@
 $EndComp
 $Comp
-L 74HC595 U?
+L 74HC595 U1
 U 1 1 5B46AB28
 P 25350 2500
-F 0 "U?" H 25500 3100 50  0000 C CNN
+F 0 "U1" H 25500 3100 50  0000 C CNN
 F 1 "74HC595" H 25350 1900 50  0000 C CNN
 F 2 "Housings_DIP:DIP-16_W7.62mm_Socket_LongPads" H 25350 2500 50  0001 C CNN
@@
 $EndComp
 $Comp
-L 74HC595 U?
+L 74HC595 U2
 U 1 1 5B46B53A
 P 25350 3900
-F 0 "U?" H 25500 4500 50  0000 C CNN
+F 0 "U2" H 25500 4500 50  0000 C CNN
 F 1 "74HC595" H 25350 3300 50  0000 C CNN
 F 2 "Housings_DIP:DIP-16_W7.62mm_Socket_LongPads" H 25350 3900 50  0001 C CNN
@@
 Text GLabel 23700 2550 0    60   Input ~ 0
 LATCH
-Text GLabel 24400 1850 1    60   Input ~ 0
-GND
-Text GLabel 24550 1850 1    60   Input ~ 0
+Text GLabel 25100 1900 2    60   Input ~ 0
 5V
 Wire Wire Line
@@
 	14200 17200 14200 16750
 Wire Wire Line
-	13250 18350 13250 17900
-Wire Wire Line
 	14200 18350 14200 17900
 Wire Wire Line
@@
 	16100 16050 16100 15600
 Wire Wire Line
-	15150 16750 15150 17200
-Wire Wire Line
 	16100 17200 16100 16750
 Wire Wire Line
@@
 	23700 2550 24650 2550
 Wire Wire Line
-	24550 1900 25050 1900
-Wire Wire Line
-	25050 1900 25050 1950
-Wire Wire Line
-	24550 2350 24650 2350
-Wire Wire Line
-	24550 1850 24550 3750
-Wire Wire Line
-	24650 2650 24400 2650
-Wire Wire Line
-	24400 1850 24400 4500
-Wire Wire Line
-	25050 3050 25050 3100
-Wire Wire Line
-	25050 3100 24400 3100
-Connection ~ 24400 2650
-Connection ~ 24550 1900
-Wire Wire Line
-	24550 3750 24650 3750
-Connection ~ 24550 2350
-Wire Wire Line
-	24400 4050 24650 4050
-Connection ~ 24400 3100
-Wire Wire Line
-	25050 4450 25050 4500
-Wire Wire Line
-	25050 4500 24400 4500
-Connection ~ 24400 4050
-Wire Wire Line
-	25050 3350 25050 3300
-Wire Wire Line
-	25050 3300 24550 3300
-Connection ~ 24550 3300
-Wire Wire Line
 	24650 3650 24150 3650
 Wire Wire Line
@@
 Text GLabel 24400 5500 0    51   Input ~ 0
 ROW_1
-$Comp
-L Conn_01x20 J?
-U 1 1 5B4A3EDA
-P 24700 6300
-F 0 "J?" H 24700 7300 50  0000 C CNN
-F 1 "Conn_01x20" H 24700 5200 50  0000 C CNN
-F 2 "" H 24700 6300 50  0001 C CNN
-F 3 "" H 24700 6300 50  0001 C CNN
-	1    24700 6300
-	1    0    0    -1
-$EndComp
 Text GLabel 24400 5600 0    51   Input ~ 0
 ROW_2
@@
 Text GLabel 24400 7200 0    51   Input ~ 0
 LATCH
+Text GLabel 24400 7500 0    51   Input ~ 0
+GND
+$Comp
+L C_Small C1
+U 1 1 5B497140
+P 25350 1500
+F 0 "C1" H 25360 1570 50  0000 L CNN
+F 1 "C_Small" H 25360 1420 50  0000 L CNN
+F 2 "Capacitors_THT:C_Disc_D5.0mm_W2.5mm_P2.50mm" H 25350 1500 50  0001 C CNN
+F 3 "" H 25350 1500 50  0001 C CNN
+	1    25350 1500
+	1    0    0    -1
+$EndComp
+Text GLabel 25350 1700 2    60   Input ~ 0
+GND
+Text GLabel 25350 1300 0    60   Input ~ 0
+5V
+Wire Wire Line
+	25350 1300 25350 1400
+Wire Wire Line
+	25350 1700 25350 1600
+Text GLabel 24550 2350 0    60   Input ~ 0
+5V
+Wire Wire Line
+	24550 2350 24650 2350
+Text GLabel 24550 2650 0    60   Input ~ 0
+GND
+Wire Wire Line
+	24550 2650 24650 2650
+Text GLabel 24900 3100 0    60   Input ~ 0
+GND
+Wire Wire Line
+	25050 3050 25050 3100
+Wire Wire Line
+	25050 3100 24900 3100
+Text GLabel 24900 4500 0    60   Input ~ 0
+GND
+Wire Wire Line
+	25050 4450 25050 4500
+Wire Wire Line
+	25050 4500 24900 4500
+Text GLabel 24550 4050 0    60   Input ~ 0
+GND
+Wire Wire Line
+	24550 4050 24650 4050
+Text GLabel 24550 3750 0    60   Input ~ 0
+5V
+Wire Wire Line
+	24550 3750 24650 3750
+Text GLabel 25100 3300 2    60   Input ~ 0
+5V
+Wire Wire Line
+	25100 1900 25050 1900
+Wire Wire Line
+	25050 1900 25050 1950
+Wire Wire Line
+	25050 3350 25050 3300
+Wire Wire Line
+	25050 3300 25100 3300
+NoConn ~ 26050 4350
+NoConn ~ 22050 2450
+NoConn ~ 22150 2450
+NoConn ~ 22250 2450
+NoConn ~ 22350 2450
+$Comp
+L Screw_Terminal_01x02 J2
+U 1 1 5B4B67A7
+P 25900 5450
+F 0 "J2" H 25900 5550 50  0000 C CNN
+F 1 "Screw_Terminal_01x02" V 26050 5400 50  0000 C CNN
+F 2 "TerminalBlocks_Phoenix:TerminalBlock_Phoenix_MPT-2.54mm_2pol" H 25900 5450 50  0001 C CNN
+F 3 "" H 25900 5450 50  0001 C CNN
+	1    25900 5450
+	1    0    0    -1
+$EndComp
+Text GLabel 25650 5600 0    60   Input ~ 0
+GND
+Text GLabel 25650 5400 0    60   Input ~ 0
+5V
+Wire Wire Line
+	25700 5300 25700 5450
+Wire Wire Line
+	25700 5400 25650 5400
+Wire Wire Line
+	25700 5550 25700 5700
+Wire Wire Line
+	25700 5600 25650 5600
+$Comp
+L Conn_01x22 J1
+U 1 1 5B4BBAF2
+P 24800 6400
+F 0 "J1" H 24800 7500 50  0000 C CNN
+F 1 "Conn_01x22" H 24800 5200 50  0000 C CNN
+F 2 "Pin_Headers:Pin_Header_Straight_1x22_Pitch2.54mm" H 24800 6400 50  0001 C CNN
+F 3 "" H 24800 6400 50  0001 C CNN
+	1    24800 6400
+	1    0    0    -1
+$EndComp
 Text GLabel 24400 7300 0    51   Input ~ 0
+DI
+Text GLabel 24400 7400 0    51   Input ~ 0
+CI
+Text GLabel 8000 2350 1    51   Input ~ 0
+DI
+Text GLabel 7900 2350 1    51   Input ~ 0
+CI
+Text GLabel 7750 2350 1    60   Input ~ 0
+5V
+Text GLabel 8150 2350 1    60   Input ~ 0
 GND
+Wire Wire Line
+	7900 2350 7900 2450
+Wire Wire Line
+	8000 2350 8000 2450
+Wire Wire Line
+	8150 2350 8100 2350
+Wire Wire Line
+	8100 2350 8100 2450
+Wire Wire Line
+	7750 2350 7800 2350
+Wire Wire Line
+	7800 2350 7800 2450
+Wire Wire Line
+	24400 5400 24600 5400
+Wire Wire Line
+	24600 5500 24400 5500
+Wire Wire Line
+	24400 5600 24600 5600
+Wire Wire Line
+	24600 5700 24400 5700
+Wire Wire Line
+	24400 5800 24600 5800
+Wire Wire Line
+	24600 5900 24400 5900
+Wire Wire Line
+	24400 6000 24600 6000
+Wire Wire Line
+	24600 6100 24400 6100
+Wire Wire Line
+	24400 6200 24600 6200
+Wire Wire Line
+	24400 6300 24600 6300
+Wire Wire Line
+	24400 6400 24600 6400
+Wire Wire Line
+	24600 6500 24400 6500
+Wire Wire Line
+	24400 6600 24600 6600
+Wire Wire Line
+	24600 6700 24400 6700
+Wire Wire Line
+	24400 6800 24600 6800
+Wire Wire Line
+	24400 6900 24600 6900
+Wire Wire Line
+	24600 7000 24400 7000
+Wire Wire Line
+	24400 7100 24600 7100
+Wire Wire Line
+	24600 7200 24400 7200
+Wire Wire Line
+	24400 7300 24600 7300
+Wire Wire Line
+	24600 7400 24400 7400
+Wire Wire Line
+	24400 7500 24600 7500
+$Comp
+L +5V #PWR01
+U 1 1 5B4D3338
+P 25700 5300
+F 0 "#PWR01" H 25700 5150 50  0001 C CNN
+F 1 "+5V" H 25700 5440 50  0000 C CNN
+F 2 "" H 25700 5300 50  0001 C CNN
+F 3 "" H 25700 5300 50  0001 C CNN
+	1    25700 5300
+	1    0    0    -1
+$EndComp
+Connection ~ 25700 5400
+$Comp
+L GND #PWR02
+U 1 1 5B4D4134
+P 25700 5700
+F 0 "#PWR02" H 25700 5450 50  0001 C CNN
+F 1 "GND" H 25700 5550 50  0000 C CNN
+F 2 "" H 25700 5700 50  0001 C CNN
+F 3 "" H 25700 5700 50  0001 C CNN
+	1    25700 5700
+	1    0    0    -1
+$EndComp
+Connection ~ 25700 5600
+Wire Wire Line
+	15150 16750 15150 17200
+Connection ~ 15150 17200
+Wire Wire Line
+	13250 17900 13250 18350
 $EndSCHEMATC

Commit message: starting bixel layout, fixed schematic symbol
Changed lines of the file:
@@
 Text GLabel 24900 4500 0    60   Input ~ 0
 GND
-Wire Wire Line
-	25050 4450 25050 4500
-Wire Wire Line
-	25050 4500 24900 4500
 Text GLabel 24550 4050 0    60   Input ~ 0
 GND
@@
 Text GLabel 25100 3300 2    60   Input ~ 0
 5V
-Wire Wire Line
-	25100 1900 25050 1900
-Wire Wire Line
-	25050 1900 25050 1950
 Wire Wire Line
 	25050 3350 25050 3300
@@
 Wire Wire Line
 	8000 2350 8000 2450
-Wire Wire Line
-	8150 2350 8100 2350
-Wire Wire Line
-	8100 2350 8100 2450
 Wire Wire Line
 	7750 2350 7800 2350
@@
 Wire Wire Line
 	13250 17900 13250 18350
+Wire Wire Line
+	24900 4500 25050 4500
+Wire Wire Line
+	25050 4500 25050 4450
+Wire Wire Line
+	25100 1900 25050 1900
+Wire Wire Line
+	25050 1900 25050 1950
+Wire Wire Line
+	8150 2350 8100 2350
+Wire Wire Line
+	8100 2350 8100 2450
 $EndSCHEMATC
